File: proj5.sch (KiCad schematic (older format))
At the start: 25 parts, among them J10 Conn_01x08_Male, J11 Conn_01x08_Male, J12 Conn_01x12_Male, J13 Conn_01x04_Male, J14 Conn_01x08_Male, J15 Conn_01x08_Male, SW1 SW_DIP_x01, SW2 SW_DIP_x01, U1 8284, U2 8086_Min_Mode, U3 74LS245, U4 74LS245, U5 74AHC373, U6 74AHC373, U7 74AHC373, Y1 Crystal

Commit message: adding changes
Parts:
- gave numbers to parts that had none: 3
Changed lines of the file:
@@
 $Descr A3 16535 11693
 encoding utf-8
-Sheet 1 3
+Sheet 1 4
 Title ""
 Date ""
@@
 	6000 1200 6000 1050
 $Comp
-L Device:C C?
+L Device:C C103
 U 1 1 60F8FF76
 P 6000 900
-F 0 "C?" H 6115 946 50  0000 L CNN
+F 0 "C103" H 6115 946 50  0000 L CNN
 F 1 "0.1uF" H 6115 855 50  0000 L CNN
 F 2 "" H 6038 750 50  0001 C CNN
@@
 $EndComp
 $Comp
-L power:GND #PWR?
+L power:GND #PWR0111
 U 1 1 60F8FF7C
 P 6000 750
-F 0 "#PWR?" H 6000 500 50  0001 C CNN
+F 0 "#PWR0111" H 6000 500 50  0001 C CNN
 F 1 "GND" H 6005 577 50  0000 C CNN
 F 2 "" H 6000 750 50  0001 C CNN
@@
 	6000 1200 6450 1200
 $Comp
-L power:VCC #PWR?
+L power:VCC #PWR0129
 U 1 1 60FF4526
 P 3800 850
-F 0 "#PWR?" H 3800 700 50  0001 C CNN
+F 0 "#PWR0129" H 3800 700 50  0001 C CNN
 F 1 "VCC" V 3815 978 50  0000 L CNN
 F 2 "" H 3800 850 50  0001 C CNN
@@
 	3550 850  3800 850
 $Comp
-L Device:C C?
+L Device:C C102
 U 1 1 60FF452F
 P 3800 700
-F 0 "C?" H 3915 746 50  0000 L CNN
+F 0 "C102" H 3915 746 50  0000 L CNN
 F 1 "0.1uF" H 3915 655 50  0000 L CNN
 F 2 "" H 3838 550 50  0001 C CNN
@@
 $EndComp
 $Comp
-L power:GND #PWR?
+L power:GND #PWR0130
 U 1 1 60FF4535
 P 3800 550
-F 0 "#PWR?" H 3800 300 50  0001 C CNN
+F 0 "#PWR0130" H 3800 300 50  0001 C CNN
 F 1 "GND" H 3805 377 50  0000 C CNN
 F 2 "" H 3800 550 50  0001 C CNN
@@
 $EndComp
 Connection ~ 3800 850
+$Comp
+L Device:C C101
+U 1 1 610306F9
+P 700 1650
+F 0 "C101" H 815 1696 50  0000 L CNN
+F 1 "100uF" H 815 1605 50  0000 L CNN
+F 2 "" H 738 1500 50  0001 C CNN
+F 3 "~" H 700 1650 50  0001 C CNN
+	1    700  1650
+	1    0    0    -1
+$EndComp
+Connection ~ 700  1500
+Wire Wire Line
+	700  1500 900  1500
+$Comp
+L power:GND #PWR0131
+U 1 1 61030F1E
+P 700 1800
+F 0 "#PWR0131" H 700 1550 50  0001 C CNN
+F 1 "GND" H 705 1627 50  0000 C CNN
+F 2 "" H 700 1800 50  0001 C CNN
+F 3 "" H 700 1800 50  0001 C CNN
+	1    700  1800
+	1    0    0    -1
+$EndComp
 Wire Bus Line
 	10050 5350 10050 6250
@@
 Wire Bus Line
 	7450 2000 7450 4100
-$Comp
-L Device:C C?
-U 1 1 610306F9
-P 700 1650
-F 0 "C?" H 815 1696 50  0000 L CNN
-F 1 "100uF" H 815 1605 50  0000 L CNN
-F 2 "" H 738 1500 50  0001 C CNN
-F 3 "~" H 700 1650 50  0001 C CNN
-	1    700  1650
-	1    0    0    -1
-$EndComp
-Connection ~ 700  1500
-Wire Wire Line
-	700  1500 900  1500
-$Comp
-L power:GND #PWR?
-U 1 1 61030F1E
-P 700 1800
-F 0 "#PWR?" H 700 1550 50  0001 C CNN
-F 1 "GND" H 705 1627 50  0000 C CNN
-F 2 "" H 700 1800 50  0001 C CNN
-F 3 "" H 700 1800 50  0001 C CNN
-	1    700  1800
-	1    0    0    -1
-$EndComp
+$Sheet
+S 9100 7550 1500 1300
+U 6095468F
+F0 "7seg&led" 50
+F1 "7seg&led.sch" 50
+$EndSheet
 $EndSCHEMATC

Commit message: cleaned up
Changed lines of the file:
@@
 $Descr A3 16535 11693
 encoding utf-8
-Sheet 1 4
+Sheet 1 5
 Title ""
 Date ""
@@
 	1    0    0    -1
 $EndComp
+$Sheet
+S 9100 7550 1500 1300
+U 6095468F
+F0 "7seg&led" 50
+F1 "7seg&led.sch" 50
+$EndSheet
 Wire Bus Line
 	10050 5350 10050 6250
@@
 	7450 2000 7450 4100
 $Sheet
-S 9100 7550 1500 1300
-U 6095468F
-F0 "7seg&led" 50
-F1 "7seg&led.sch" 50
+S 6650 7850 1300 1200
+U 6095B35F
+F0 "8254_and_LCD" 50
+F1 "8254_and_LCD.sch" 50
 $EndSheet
 $EndSCHEMATC

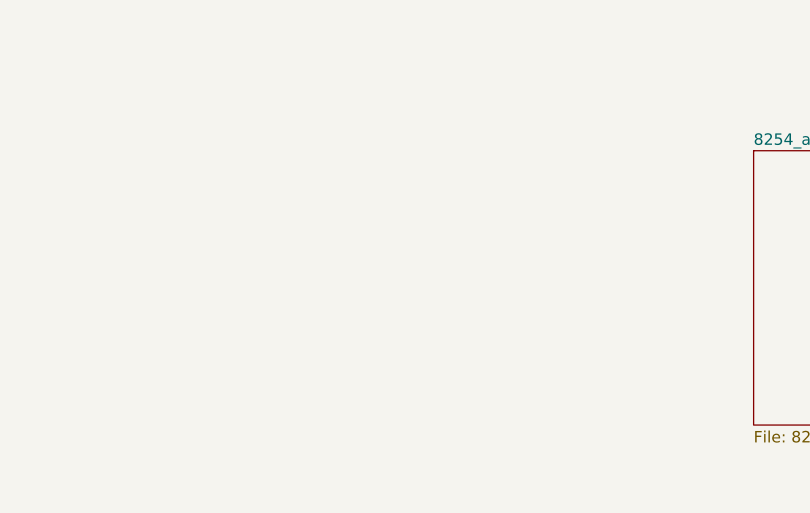
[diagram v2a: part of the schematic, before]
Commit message: tweeked cy7119_and_28f010.sch
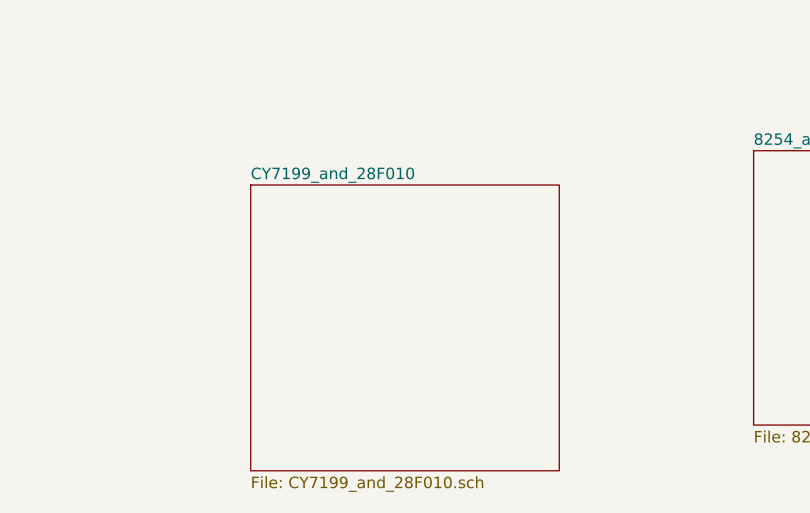
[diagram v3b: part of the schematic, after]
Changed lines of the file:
@@
 $Descr A3 16535 11693
 encoding utf-8
-Sheet 1 5
+Sheet 1 6
 Title ""
 Date ""
@@
 F1 "7seg&led.sch" 50
 $EndSheet
+$Sheet
+S 6650 7850 1300 1200
+U 6095B35F
+F0 "8254_and_LCD" 50
+F1 "8254_and_LCD.sch" 50
+$EndSheet
+$Sheet
+S 4450 8000 1350 1250
+U 60997B77
+F0 "CY7199_and_28F010" 50
+F1 "CY7199_and_28F010.sch" 50
+$EndSheet
 Wire Bus Line
 	10050 5350 10050 6250
@@
 Wire Bus Line
 	7450 2000 7450 4100
-$Sheet
-S 6650 7850 1300 1200
-U 6095B35F
-F0 "8254_and_LCD" 50
-F1 "8254_and_LCD.sch" 50
-$EndSheet
 $EndSCHEMATC

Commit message: tweaked a few things
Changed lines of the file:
@@
 L power:GND #PWR0131
 U 1 1 61030F1E
-P 700 1800
-F 0 "#PWR0131" H 700 1550 50  0001 C CNN
-F 1 "GND" H 705 1627 50  0000 C CNN
-F 2 "" H 700 1800 50  0001 C CNN
-F 3 "" H 700 1800 50  0001 C CNN
-	1    700  1800
+P 700 2000
+F 0 "#PWR0131" H 700 1750 50  0001 C CNN
+F 1 "GND" H 705 1827 50  0000 C CNN
+F 2 "" H 700 2000 50  0001 C CNN
+F 3 "" H 700 2000 50  0001 C CNN
+	1    700  2000
 	1    0    0    -1
 $EndComp
@@
 Wire Bus Line
 	7450 2000 7450 4100
+Wire Wire Line
+	700  1800 700  2000
 $EndSCHEMATC

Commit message: made final adjustments to all the designes
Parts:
- removed SW1: SW_DIP_x01, Button_Switch_THT:SW_PUSH-12mm, symbol Switch:SW_DIP_x01
- removed SW2: SW_DIP_x01, symbol Switch:SW_DIP_x01
- removed U5: 74AHC373, symbol 74xx:74AHC373
- added J101: Screw_Terminal_01x02, TerminalBlock_4Ucon:TerminalBlock_4Ucon_1x02_P3.50mm_Horizontal, symbol Connector:Screw_Terminal_01x02
- added SW101, SW102: SW_Push, Button_Switch_SMD:SW_SPST_B3U-1000P, symbol Switch:SW_Push
- added U105: 74LS373, Package_DIP:DIP-20_W7.62mm_SMDSocket_SmallPads, symbol 74xx:74LS373
- C101: renamed from C2; footprint (none) -> Capacitor_SMD:CP_Elec_5x3
- C102: renamed from C101; footprint (none) -> Capacitor_SMD:CP_Elec_8x5.4
- C103: renamed from C1; footprint Capacitor_THT:CP_Axial_L10.0mm_D4.5mm_P15.00mm_Horizontal -> Capacitor_SMD:CP_Elec_5x3
- C104: renamed from C102; footprint (none) -> Capacitor_SMD:CP_Elec_3x5.3
- C105: renamed from C103; footprint (none) -> Capacitor_SMD:CP_Elec_3x5.3
- D101: renamed from D2; footprint (none) -> Diode_SMD:D_0402_1005Metric
- D102: renamed from D1; footprint (none) -> Diode_SMD:D_0402_1005Metric
- J102: renamed from J10; footprint (none) -> Connector_JST:JST_GH_BM08B-GHS-TBT_1x08-1MP_P1.25mm_Vertical
- J103: renamed from J11; footprint (none) -> Connector_JST:JST_GH_BM08B-GHS-TBT_1x08-1MP_P1.25mm_Vertical
- J104: renamed from J12; footprint (none) -> Connector_JST:JST_GH_BM12B-GHS-TBT_1x12-1MP_P1.25mm_Vertical
- J105: renamed from J13; footprint (none) -> Connector_JST:JST_GH_BM04B-GHS-TBT_1x04-1MP_P1.25mm_Vertical
- J106: renamed from J14; footprint (none) -> Connector_JST:JST_GH_BM08B-GHS-TBT_1x08-1MP_P1.25mm_Vertical
- J107: renamed from J15; footprint (none) -> Connector_JST:JST_GH_BM08B-GHS-TBT_1x08-1MP_P1.25mm_Vertical
- R101: renamed from R2; value R_US -> 10k; footprint (none) -> Resistor_SMD:R_0402_1005Metric
- R102: renamed from R1; footprint Resistor_THT:R_Axial_DIN0204_L3.6mm_D1.6mm_P1.90mm_Vertical -> Resistor_SMD:R_0402_1005Metric
- U101: renamed from U3; footprint (none) -> Package_DIP:DIP-20_W7.62mm_SMDSocket_SmallPads
- U102: renamed from U4; footprint (none) -> Package_DIP:DIP-20_W7.62mm_SMDSocket_SmallPads
- U106: renamed from U6; footprint (none) -> Package_DIP:DIP-20_W7.62mm_SMDSocket_SmallPads
- U107: renamed from U7; footprint (none) -> Package_DIP:DIP-20_W7.62mm_SMDSocket_SmallPads
- renumbered U1 to U103, U2 to U104, Y1 to Y101
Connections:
- net +5V: now also J101.2 (Pin_2), SW101.1, U105.20 (VCC)
- net A0: now also U105.2 (O0)
- net A1: now also U105.5 (O1)
- net A2: now also U105.6 (O2)
- net A3: now also U105.9 (O3)
- net A4: now also U105.12 (O4)
- net A5: now also U105.15 (O5)
- net A6: now also U105.16 (O6)
- net A7: now also U105.19 (O7)
- net AD0: now also U105.3 (D0)
- net AD1: now also U105.4 (D1)
- net AD2: now also U105.7 (D2)
- net AD3: now also U105.8 (D3)
- net AD4: now also U105.13 (D4)
- net AD5: now also U105.14 (D5)
- net AD6: now also U105.17 (D6)
- net AD7: now also U105.18 (D7)
- net ALE: now also U105.11 (LE)
- net GND: now also J101.1 (Pin_1), SW102.1, U105.1 (OE), U105.10 (GND)
- net NMI: now also SW101.2
- net at C103.1, D102.1 (A), R102.2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: now also SW102.2
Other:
- moved on the sheet: C102

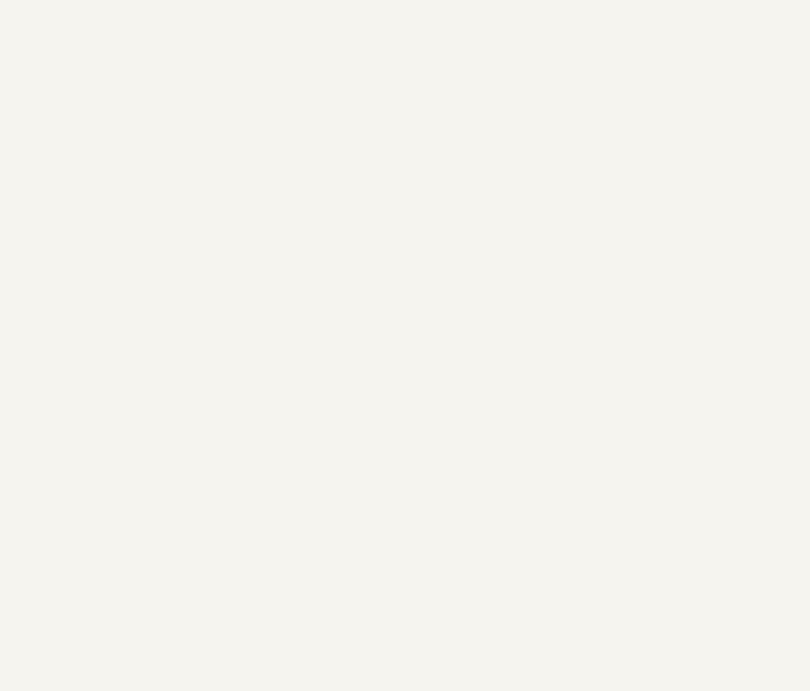
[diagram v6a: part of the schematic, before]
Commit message: adjusted and incorperated 8dipswitch to pcb
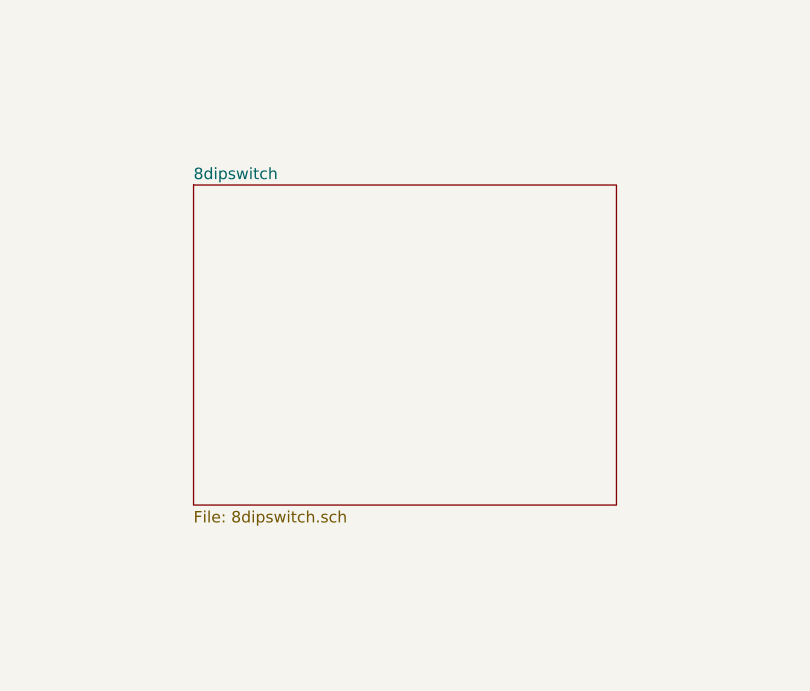
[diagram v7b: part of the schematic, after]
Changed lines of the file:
@@
 $Descr A3 16535 11693
 encoding utf-8
-Sheet 1 8
+Sheet 1 9
 Title ""
 Date ""
@@
 Wire Bus Line
 	7450 2000 7450 4100
+$Sheet
+S 6150 8450 1850 1400
+U 60AD5691
+F0 "8dipswitch" 50
+F1 "8dipswitch.sch" 50
+$EndSheet
 $EndSCHEMATC

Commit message: finished pcb layout
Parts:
- J101: footprint TerminalBlock_4Ucon:TerminalBlock_4Ucon_1x02_P3.50mm_Horizontal -> TerminalBlock_Phoenix:TerminalBlock_Phoenix_MKDS-1,5-2-5.08_1x02_P5.08mm_Horizontal
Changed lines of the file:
@@
 F 0 "J101" V 1264 8862 50  0000 R CNN
 F 1 "Screw_Terminal_01x02" V 1173 8862 50  0000 R CNN
-F 2 "TerminalBlock_4Ucon:TerminalBlock_4Ucon_1x02_P3.50mm_Horizontal" H 1300 9050 50  0001 C CNN
+F 2 "TerminalBlock_Phoenix:TerminalBlock_Phoenix_MKDS-1,5-2-5.08_1x02_P5.08mm_Horizontal" H 1300 9050 50  0001 C CNN
 F 3 "~" H 1300 9050 50  0001 C CNN
 	1    1300 9050
